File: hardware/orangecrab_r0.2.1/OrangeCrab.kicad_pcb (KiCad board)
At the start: 6 copper layers, 42 x 22 mm, 97 parts, among them J6 Conn_01x05, U1 TLV62569DRL, U10 NCP115-2.5, U2 TLV62569DRL, U3 LFE5U-25F-8MG285C, U4 MT41K64M16TW-107_J-TR, U6 W25Q128JVP, U7 TLV62569DRL

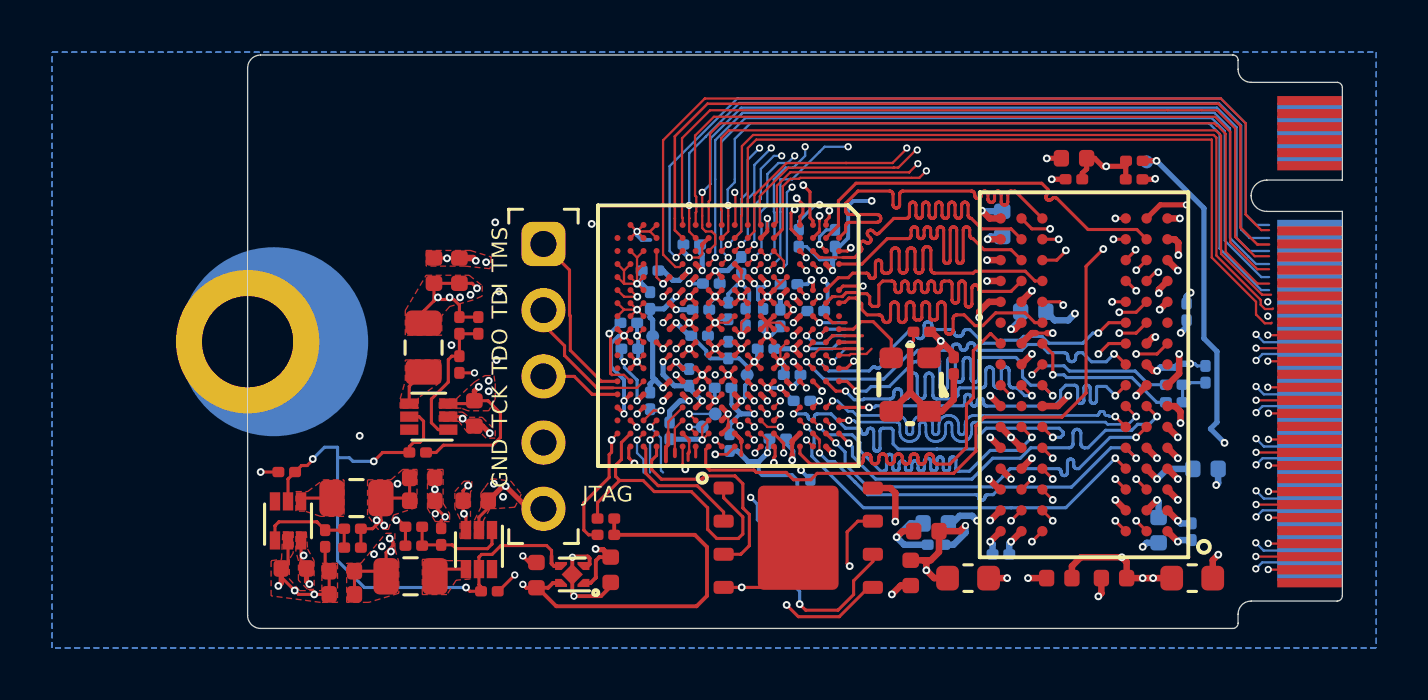
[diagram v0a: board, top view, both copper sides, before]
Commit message: route done except final pinswap
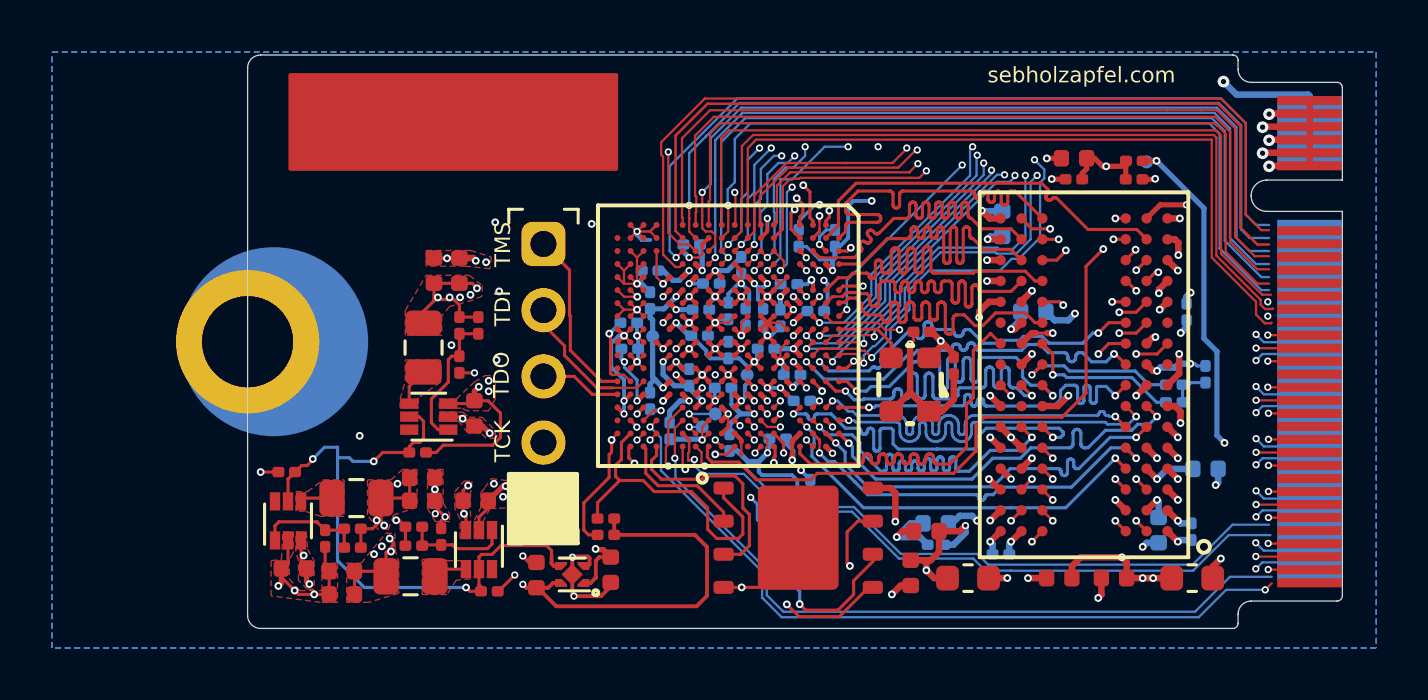
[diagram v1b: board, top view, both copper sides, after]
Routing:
- net VSYS: track 29.0 -> 74.1 mm, vias 10 -> 11
- net 3V3_IO18_M3: track 2.19 -> 47.1 mm, vias 1 -> 2
- net 3V3_IO37_B8: track 2.47 -> 44.3 mm, vias 1 -> 3
- net 3V3_IO29_C11: track 3.59 -> 40.3 mm, vias 1 -> 3
- net 3V3_IO30_A11: track 1.35 -> 37.7 mm, vias 0 -> 2
- net 3V3_IO32_B10: track 1.51 -> 37.1 mm, vias 0 -> 2
- net 3V3_IO3_F3: track 4.35 -> 38.7 mm
- net 3V3_IO33_C10: track 3.54 -> 35.1 mm, vias 2 -> 3
- net 3V3_IO31_A10: track 0.75 -> 32.1 mm, vias 0 -> 2
- net 3V3_IO36_A8: track 2.17 -> 33.3 mm, vias 1 -> 3
- net 3V3_IO28_B11: track 3.74 -> 34.6 mm, vias 2 -> 3
- net 3V3_IO35_C9: track 4.16 -> 35.0 mm, vias 2 -> 3
- net 3V3_IO34_B9: track 3.65 -> 34.0 mm, vias 2 -> 3
- net 3V3_IO38_C8: track 1.35 -> 31.6 mm, vias 1 -> 2
- net 3V3_IO44_T17: track 3.88 -> 31.4 mm
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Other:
- board text added: "applecrab"
- board text added: "r0.1"
- board text added: "sebholzapfel.com"
- board text removed: "GND"
- board text removed: "JTAG"

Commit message: execute pinswap, not routed yet
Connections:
- U$1 pad P$20: 3V3_IO0_H4 -> 3V3_IO17_N3
- U$1 pad P$21: 3V3_IO1_G4 -> 3V3_IO16_N4
- U$1 pad P$22: 3V3_IO2_F4 -> 3V3_IO24_M2
- U$1 pad P$23: 3V3_IO3_F3 -> 3V3_IO25_N2
- U$1 pad P$24: 3V3_IO4_H3 -> 3V3_IO19_L3
- U$1 pad P$25: 3V3_IO5_G3 -> 3V3_IO27_N1
- U$1 pad P$26: 3V3_IO6_J3 -> 3V3_IO15_L4
- U$1 pad P$27: 3V3_IO7_H2 -> 3V3_IO26_M1
- U$1 pad P$28: 3V3_IO8_F2 -> 3V3_IO14_K4
- U$1 pad P$29: 3V3_IO9_G1 -> 3V3_IO23_L1
- U$1 pad P$30: 3V3_IO10_J2 -> 3V3_IO22_K2
- U$1 pad P$31: 3V3_IO11_J1 -> 3V3_IO21_K1
- U$1 pad P$32: 3V3_IO12_F1 -> 3V3_IO1_G4
- U$1 pad P$33: 3V3_IO13_H1 -> 3V3_IO10_J2
- U$1 pad P$34: 3V3_IO14_K4 -> 3V3_IO11_J1
- U$1 pad P$35: 3V3_IO15_L4 -> 3V3_IO13_H1
- U$1 pad P$36: 3V3_IO16_N4 -> unconnected-(U$1-36-PadP$36)
- U$1 pad P$37: 3V3_IO17_N3 -> 3V3_IO20_K3
- U$1 pad P$38: 3V3_IO18_M3 -> 3V3_IO6_J3
- U$1 pad P$39: 3V3_IO19_L3 -> 3V3_IO4_H3
- U$1 pad P$40: 3V3_IO20_K3 -> 3V3_IO0_H4
- U$1 pad P$41: 3V3_IO21_K1 -> 3V3_IO5_G3
- U$1 pad P$42: 3V3_IO22_K2 -> unconnected-(U$1-42-PadP$42)
- U$1 pad P$43: 3V3_IO23_L1 -> unconnected-(U$1-43-PadP$43)
- U$1 pad P$44: 3V3_IO24_M2 -> unconnected-(U$1-44-PadP$44)
- U$1 pad P$45: 3V3_IO25_N2 -> 3V3_IO2_F4
- U$1 pad P$46: 3V3_IO26_M1 -> 3V3_IO7_H2
- U$1 pad P$47: 3V3_IO27_N1 -> 3V3_IO9_G1
- U$1 pad P$48: 3V3_IO28_B11 -> 3V3_IO12_F1
- U$1 pad P$49: 3V3_IO29_C11 -> 3V3_IO8_F2
- U$1 pad P$50: 3V3_IO30_A11 -> unconnected-(U$1-50-PadP$50)
- U$1 pad P$51: 3V3_IO31_A10 -> unconnected-(U$1-51-PadP$51)
- U$1 pad P$52: 3V3_IO32_B10 -> unconnected-(U$1-52-PadP$52)
- U$1 pad P$53: 3V3_IO33_C10 -> 3V3_IO36_A8
- U$1 pad P$54: 3V3_IO34_B9 -> 3V3_IO38_C8
- U$1 pad P$55: 3V3_IO35_C9 -> 3V3_IO34_B9
- U$1 pad P$56: 3V3_IO36_A8 -> 3V3_IO35_C9
- U$1 pad P$57: 3V3_IO37_B8 -> 3V3_IO33_C10
- U$1 pad P$58: 3V3_IO38_C8 -> unconnected-(U$1-58-PadP$58)
- U$1 pad P$59: 3V3_IO39_N15 -> unconnected-(U$1-59-PadP$59)
- U$1 pad P$60: 3V3_IO40_N16 -> 3V3_IO39_N15
- U$1 pad P$61: 3V3_IO41_N17 -> 3V3_IO28_B11
- U$1 pad P$62: 3V3_IO42_M18 -> 3V3_IO31_A10
- U$1 pad P$63: 3V3_IO43_R17 -> 3V3_IO32_B10
- U$1 pad P$64: 3V3_IO44_T17 -> 3V3_IO29_C11
- U$1 pad P$65: 3V3_IO45_R16 -> 3V3_IO30_A11
- U$1 pad P$66: unconnected-(U$1-66-PadP$66) -> 3V3_IO42_M18
- U$1 pad P$68: unconnected-(U$1-68-PadP$68) -> 3V3_IO41_N17
- U$1 pad P$69: unconnected-(U$1-69-PadP$69) -> 3V3_IO18_M3
- U$1 pad P$70: unconnected-(U$1-70-PadP$70) -> 3V3_IO3_F3
- U$1 pad P$71: unconnected-(U$1-71-PadP$71) -> 3V3_IO37_B8
- U$1 pad P$72: unconnected-(U$1-72-PadP$72) -> 3V3_IO43_R17
- U$1 pad P$73: unconnected-(U$1-73-PadP$73) -> 3V3_IO44_T17
- U$1 pad P$74: unconnected-(U$1-74-PadP$74) -> 3V3_IO40_N16
- U$1 pad P$75: unconnected-(U$1-75-PadP$75) -> 3V3_IO45_R16
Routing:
- net 3V3_IO31_A10: track 32.1 -> 34.3 mm, vias 2 -> 3
- net 3V3_IO26_M1: track 32.9 -> 30.7 mm, vias 1 -> 0
- net 3V3_IO7_H2: track 32.3 -> 34.5 mm, vias 1 -> 2
- net 3V3_IO6_J3: track 31.1 -> 33.3 mm, vias 2 -> 3
- net 3V3_IO42_M18: track 26.9 -> 24.7 mm, vias 2 -> 1
- net 3V3_IO38_C8: track 31.6 -> 33.8 mm, vias 2 -> 3
- net 3V3_IO0_H4: track 31.7 -> 33.8 mm, vias 2 -> 3
- net 3V3_IO12_F1: track 31.4 -> 33.5 mm, vias 1 -> 2
- net unconnected-(U$1-70-PadP$70): track 2.17 -> 0.00 mm, vias 1 -> 0
- net 3V3_IO3_F3: track 38.7 -> 40.8 mm, vias 2 -> 3
- net unconnected-(U$1-72-PadP$72): track 2.13 -> 0.00 mm, vias 1 -> 0
- net unconnected-(U$1-71-PadP$71): track 2.06 -> 0.00 mm, vias 1 -> 0
- net 3V3_IO19_L3: track 33.7 -> 31.6 mm, vias 2 -> 1
- net 3V3_IO9_G1: track 31.6 -> 33.6 mm, vias 1 -> 2
- net 3V3_IO32_B10: track 37.1 -> 39.2 mm, vias 2 -> 3
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
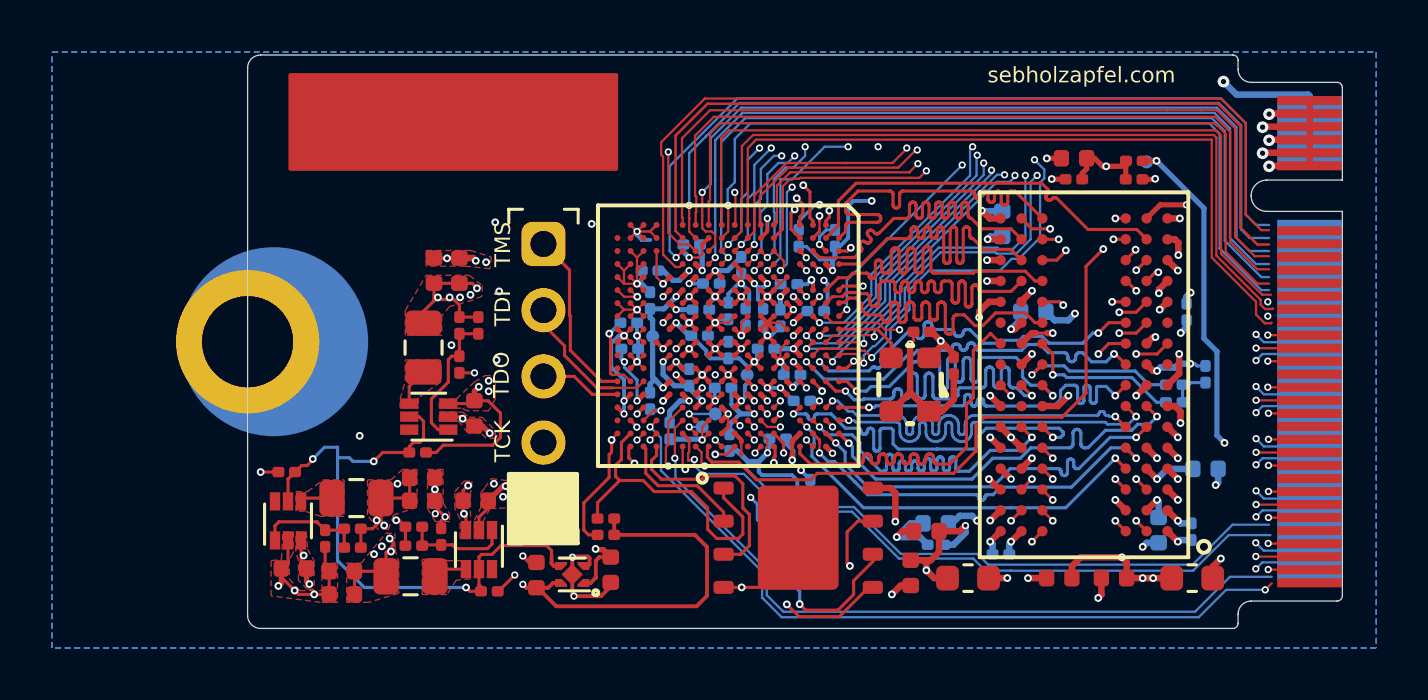
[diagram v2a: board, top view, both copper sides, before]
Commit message: complete route, clear all DRC violations
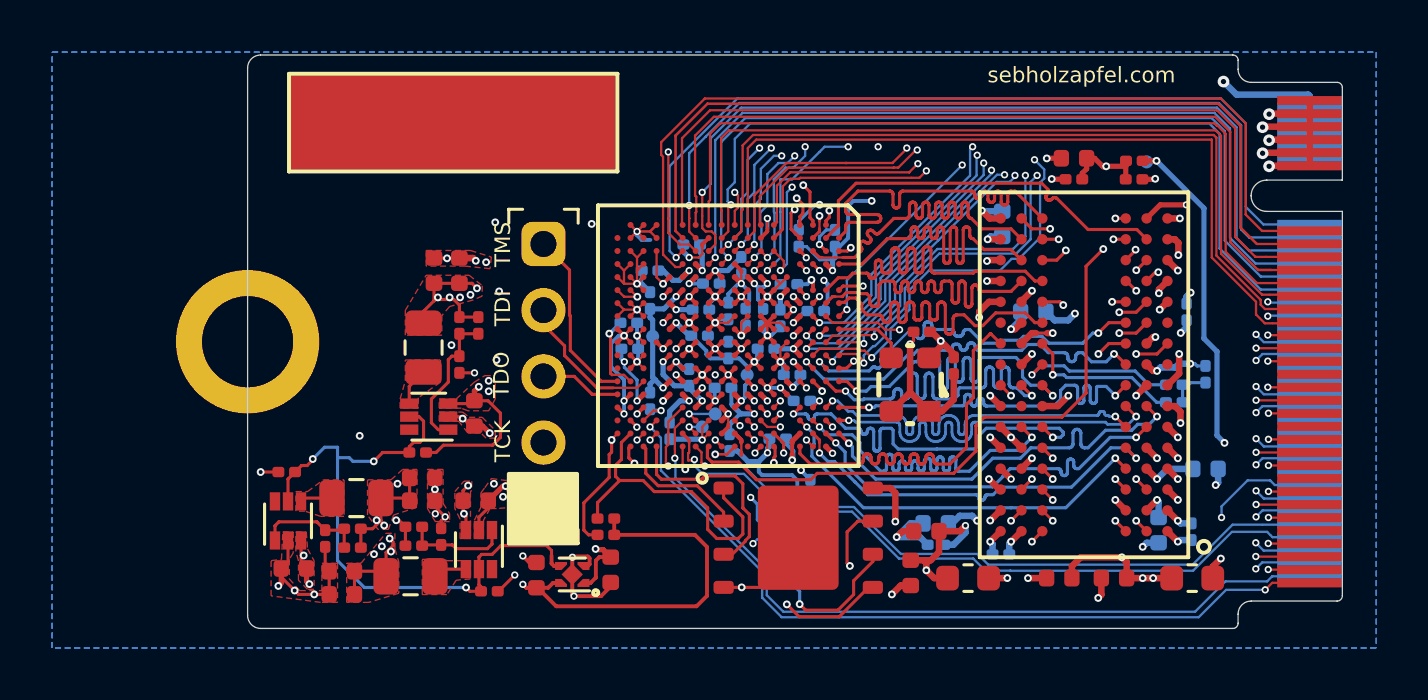
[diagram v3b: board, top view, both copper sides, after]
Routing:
- net 3V3_IO39_N15: track 27.6 -> 33.6 mm, vias 1 -> 2
- net 3V3_IO26_M1: track 30.7 -> 32.8 mm
- net 3V3_IO11_J1: track 31.0 -> 32.7 mm
- net 3V3_IO41_N17: track 26.0 -> 27.6 mm
- net 3V3_IO22_K2: track 30.0 -> 31.6 mm
- net 3V3_IO1_G4: track 44.7 -> 46.3 mm
- net 3V3_IO16_N4: track 33.5 -> 35.1 mm
- net 3V3_IO27_N1: track 31.1 -> 32.6 mm
- net 3V3_IO42_M18: track 24.7 -> 26.3 mm
- net 3V3_IO14_K4: track 31.3 -> 32.8 mm
- net 3V3_IO25_N2: track 31.8 -> 33.4 mm
- net 3V3_IO24_M2: track 30.9 -> 32.5 mm
- net 3V3_IO23_L1: track 30.3 -> 31.9 mm
- net 3V3_IO19_L3: track 31.6 -> 33.1 mm
- net 3V3_IO15_L4: track 31.4 -> 33.0 mm
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
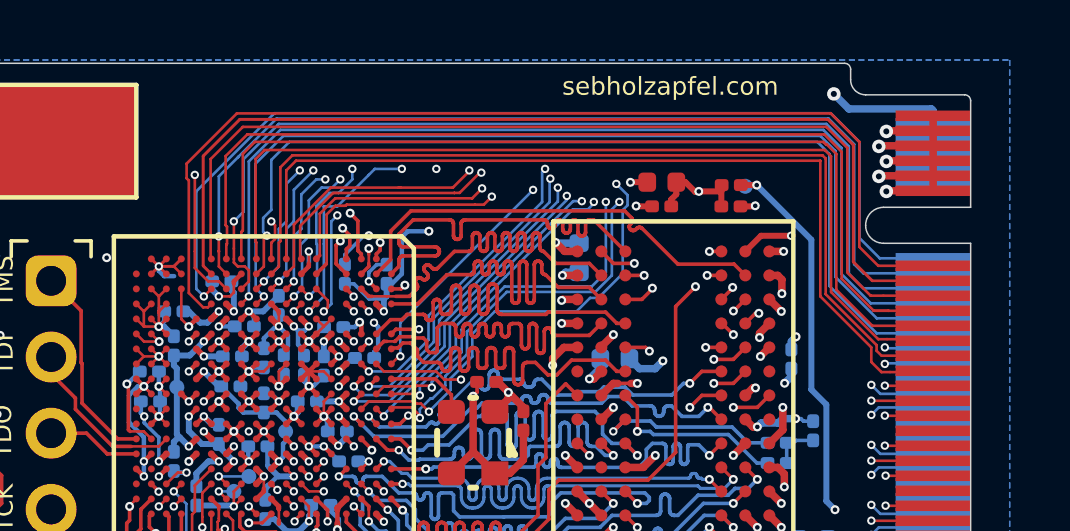
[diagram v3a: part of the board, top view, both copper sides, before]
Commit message: Clean up traces and silk
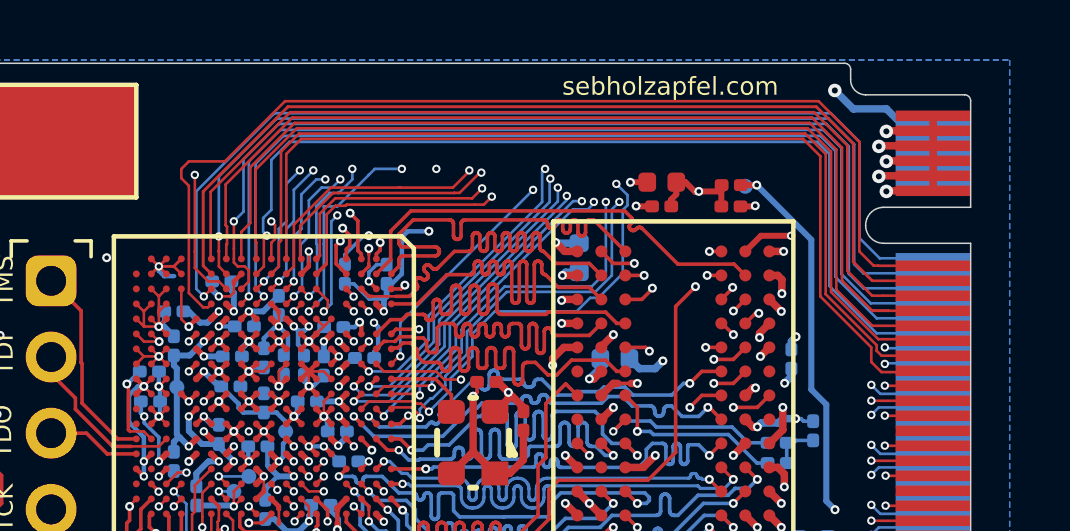
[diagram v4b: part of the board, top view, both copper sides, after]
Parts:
- added REF**: OSHW-Symbol_6.7x6mm_SilkScreen, Symbol:OSHW-Symbol_6.7x6mm_SilkScreen, B.Cu at (148.8, 96.7)
- added REF**: WEEE-Logo_4.2x6mm_SilkScreen, Symbol:WEEE-Logo_4.2x6mm_SilkScreen, B.Cu at (148.8, 108.3)
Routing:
- net 3V3_IO13_H1: track 30.5 -> 31.5 mm
- net 3V3_IO10_J2: track 31.1 -> 32.1 mm
- net 3V3_IO16_N4: track 35.1 -> 35.6 mm
